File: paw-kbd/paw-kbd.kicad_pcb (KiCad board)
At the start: 2 copper layers, 130.8 x 88.1 mm, 55 parts, among them J1 OLED, J2 TRRS, J3 TRACKBALL, SW1 SW_PUSH, SW10 SW_PUSH, SW11 SW_PUSH, SW12 SW_PUSH, SW13 SW_PUSH, SW14 SW_PUSH, SW15 SW_PUSH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

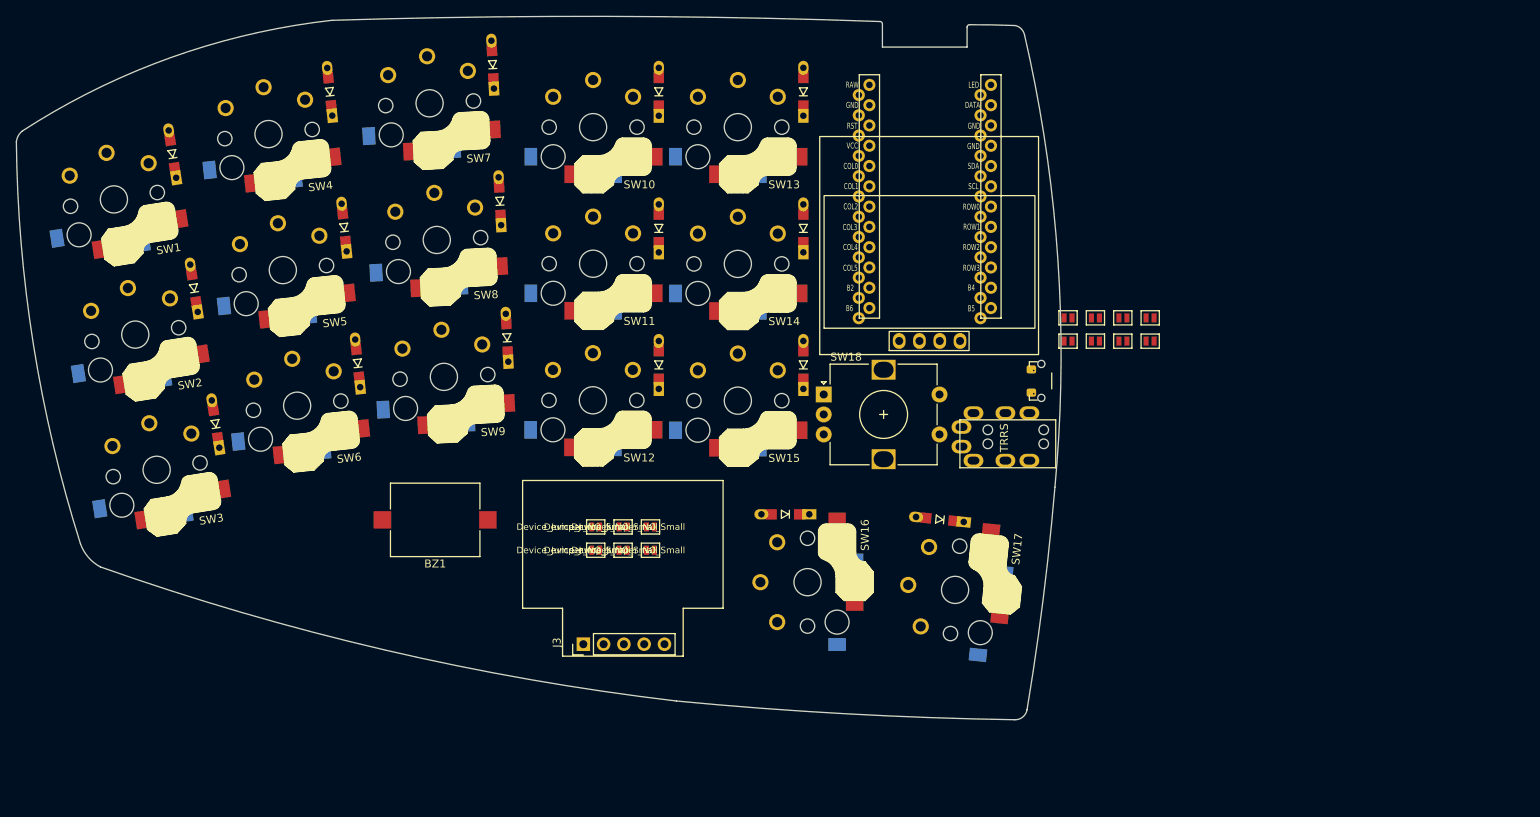
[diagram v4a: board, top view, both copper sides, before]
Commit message: big oled
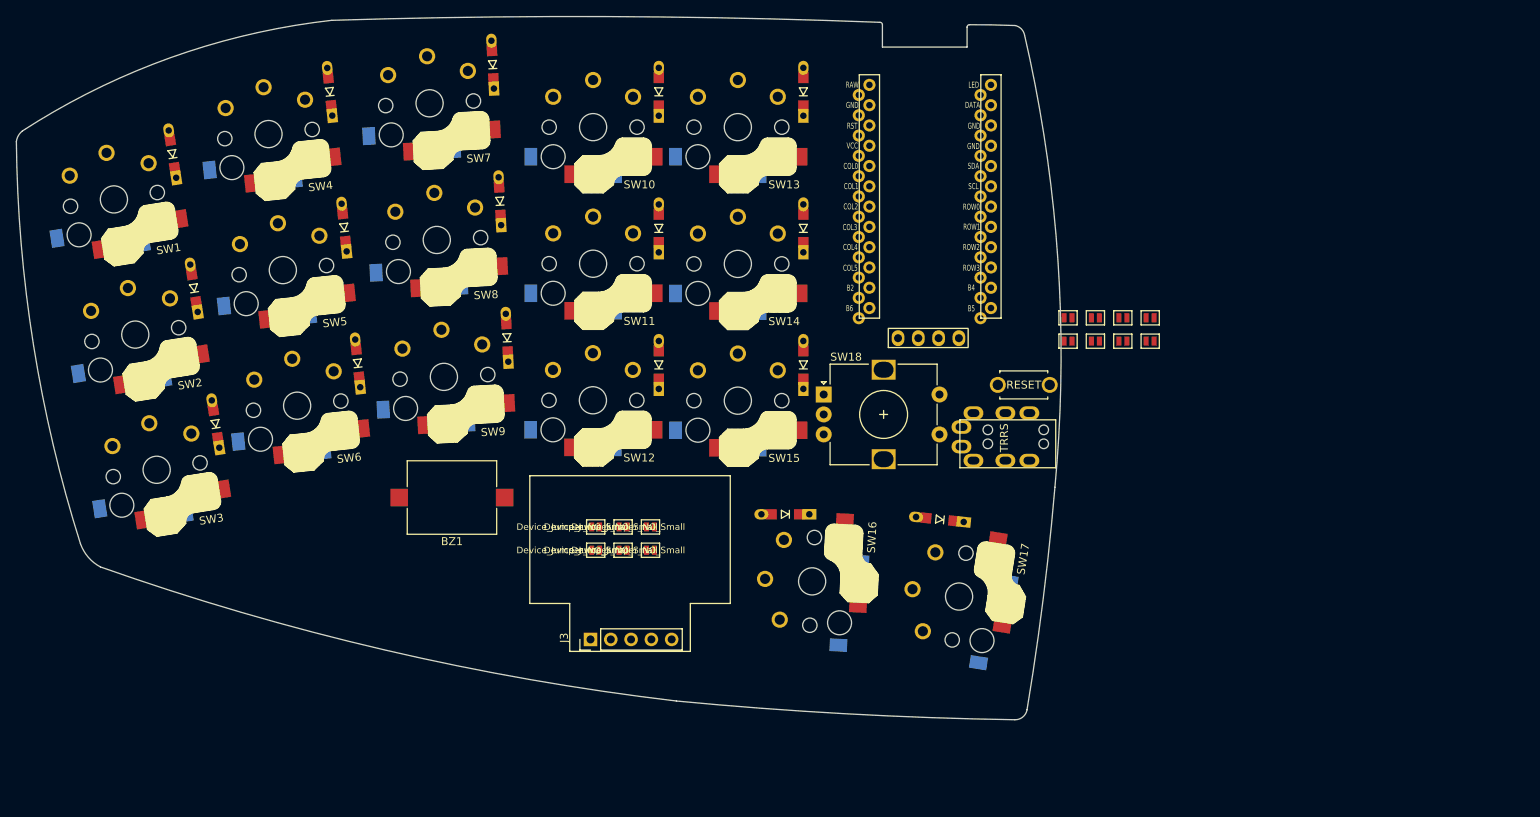
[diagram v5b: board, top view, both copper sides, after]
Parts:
- RSW1: footprint keeb-footprints:SW_Push_1P1T-MP_NO_Horizontal_both_sides -> kbd:ResetSW
- moved BZ1 3.50 mm to (139.5, 110.4)
- moved RSW1 2.26 mm to (211.1, 96.3), turned to 0 degrees
- moved J3 1.08 mm to (156.8, 128.2)
- moved SW17 0.97 mm to (203.0, 122.8), turned to 81 degrees
- moved SW16 0.58 mm to (184.6, 120.9), turned to 87 degrees
- moved J1 0.39 mm to (199.2, 80.4)
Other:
- board size 130.8 x 88.1 mm -> 130.8 x 88 mm

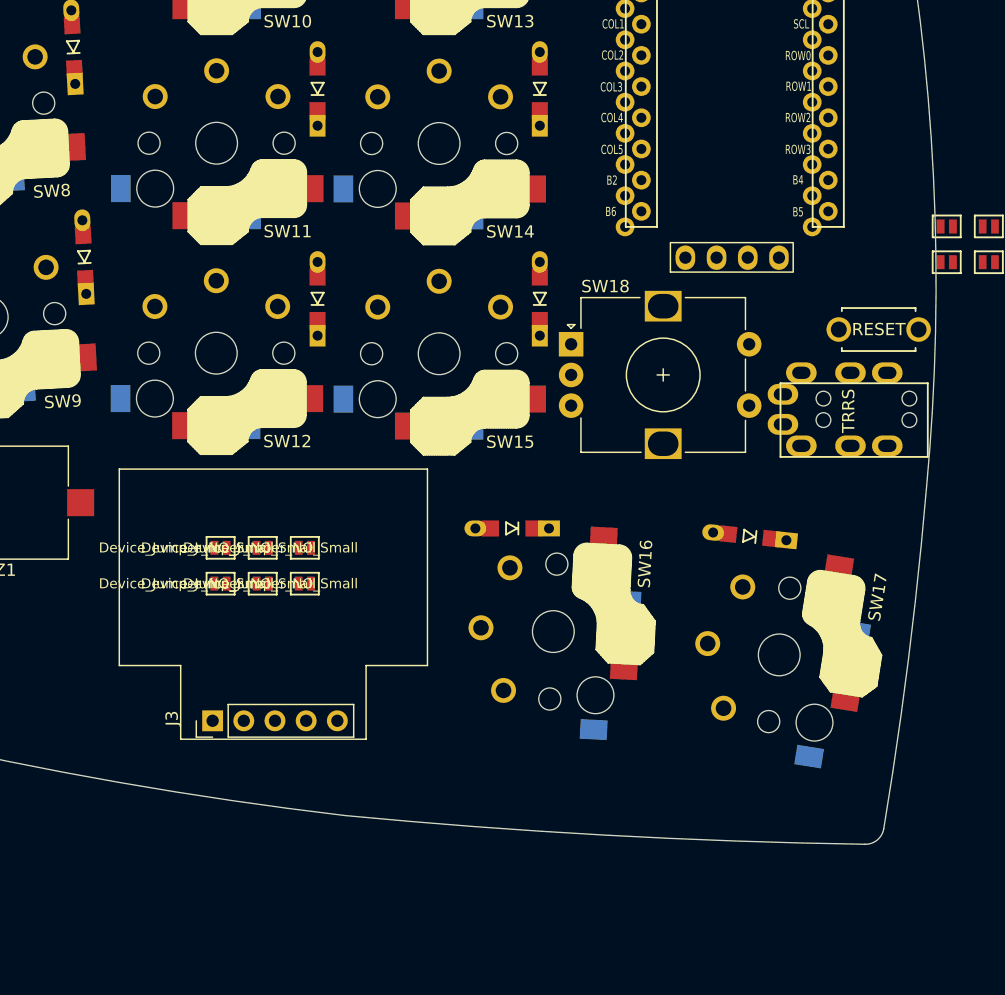
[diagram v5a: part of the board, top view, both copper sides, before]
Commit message: pimoroni trackball footprint
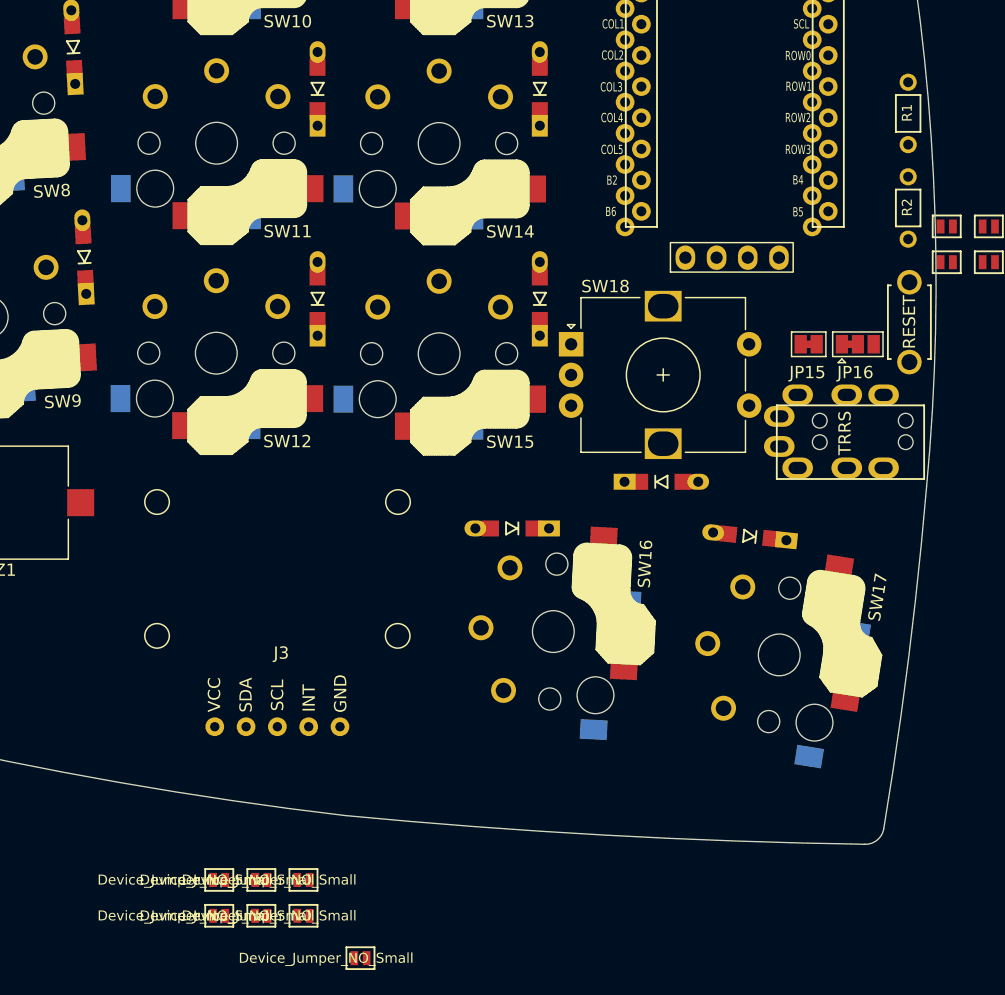
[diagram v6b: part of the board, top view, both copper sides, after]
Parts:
- added D18: DIODE, kbd:D3_TH_SMD_v2, F.Cu at (193.4, 108.7)
- added JP15: Jumper_2_Bridged, Jumper:SolderJumper-2_P1.3mm_Bridged_Pad1.0x1.5mm, F.Cu at (205.4, 97.5)
- added JP16: Jumper_3_Bridged12, Jumper:SolderJumper-3_P1.3mm_Bridged12_Pad1.0x1.5mm, F.Cu at (209.4, 97.5)
- added JP17: Device_Jumper_NO_Small, kbd:Jumper, F.Cu at (168.9, 147.5)
- added R1: R, kbd:R, F.Cu at (213.5, 78.7)
- added R2: R, kbd:R, F.Cu at (213.5, 86.4)
- J3: footprint keeb-footprints:pimoroni -> keeb-footprints:pimoroni_trackball
- moved JP11 27.1 mm to (160.8, 144.1)
- moved JP13 27.1 mm to (164.2, 144.1)
- moved JP9 27.1 mm to (157.4, 144.1)
- moved JP10 27.1 mm to (157.4, 141.1)
- moved JP12 27.1 mm to (164.2, 141.1)
- moved JP14 27.1 mm to (160.8, 141.1)
- moved J3 13.5 mm to (162.1, 115.8), turned to 0 degrees
- moved RSW1 2.57 mm to (213.6, 95.7), turned to 90 degrees
- moved J2 1.82 mm to (214.8, 105.5)
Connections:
- D1 pad 2: Net-(D1-Pad2) -> top
- D10 pad 2: Net-(D1-Pad2) -> top
- D11 pad 2: Net-(D11-Pad2) -> home
- D12 pad 2: Net-(D12-Pad2) -> bottom
- D14 pad 2: Net-(D1-Pad2) -> top
- D15 pad 2: Net-(D11-Pad2) -> home
- D16 pad 2: Net-(D12-Pad2) -> bottom
- D2 pad 2: Net-(D11-Pad2) -> home
- D3 pad 2: Net-(D12-Pad2) -> bottom
- D4 pad 2: Net-(D1-Pad2) -> top
- D5 pad 2: Net-(D11-Pad2) -> home
- D6 pad 2: Net-(D12-Pad2) -> bottom
- D7 pad 2: Net-(D1-Pad2) -> top
- D8 pad 2: Net-(D11-Pad2) -> home
- D9 pad 2: Net-(D12-Pad2) -> bottom
- J3 pad 1: Net-(J3-Pad1) -> Net-(JP11-Pad1)
- J3 pad 3: VCC -> Net-(J3-Pad3)
- J3 pad 4: Net-(J3-Pad4) -> Net-(JP14-Pad1)
- JP10 pad 1: Net-(J3-Pad2) -> Net-(J3-Pad3)
- JP11 pad 1: Net-(J3-Pad4) -> Net-(JP11-Pad1)
- JP11 pad 2: GND -> VCC
- JP12 pad 1: Net-(J3-Pad2) -> Net-(JP11-Pad1)
- JP13 pad 1: Net-(J3-Pad4) -> Net-(J3-Pad5)
- JP13 pad 2: SCL -> GND
- JP14 pad 1: Net-(J3-Pad5) -> Net-(JP14-Pad1)
- JP9 pad 1: Net-(J3-Pad1) -> Net-(J3-Pad2)
- SW1 pad 1: col1 -> pinky
- SW10 pad 1: col4 -> index
- SW11 pad 1: col4 -> index
- SW12 pad 1: col4 -> index
- SW13 pad 1: col5 -> far
- SW14 pad 1: col5 -> far
- SW15 pad 1: col5 -> far
- SW16 pad 1: col4 -> index
- SW17 pad 1: col5 -> far
- SW2 pad 1: col1 -> pinky
- SW3 pad 1: col1 -> pinky
- SW4 pad 1: col2 -> ring
- SW5 pad 1: col2 -> ring
- SW6 pad 1: col2 -> ring
- SW7 pad 1: col3 -> SW18A
- SW8 pad 1: col3 -> SW18A
- SW9 pad 1: col3 -> SW18A
- U1 pad 1: col5 -> AUDIO
- U1 pad 10: col1 -> ring
- U1 pad 11: col0 -> pinky
- U1 pad 12: thumb -> unconnected-(U1-Pad12)
- U1 pad 13: unconnected-(U1-Pad13) -> ENCA
- U1 pad 14: unconnected-(U1-Pad14) -> ENCB
- U1 pad 17: unconnected-(U1-Pad17) -> thumb
- U1 pad 7: col4 -> far
- U1 pad 8: col3 -> index
- U1 pad 9: col2 -> SW18A

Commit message: 2023-07-29 15:25:01
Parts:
- added D18: type="D" model="DIODE" lib="", kbd:D3_TH_SMD_v2, F.Cu at (244.2, 90.2)
- added SW18: SW_PUSH, keeb-footprints:ChocV1_V2_Hotswap_optional_reversed_choc_spacing, F.Cu at (204.9, 120.0)
- D1, D10, D11, D12, D13, D14, D15, D16, D17, D2, D3, D4, D5, D6, D7, D8, D9: value DIODE -> type="D" model="DIODE" lib=""
- SW16, SW17: footprint keeb-footprints:ChocV1_V2_Hotswap_optional_reversed_15u_choc_spacing -> keeb-footprints:ChocV1_V2_Hotswap_optional_reversed_choc_spacing
- moved BZ1 122.3 mm to (256.6, 75.0)
- moved JP17 99.1 mm to (267.5, 137.8)
- moved JP10 99.1 mm to (256.0, 131.4)
- moved JP9 99.1 mm to (256.0, 134.3)
- moved JP11 99.1 mm to (259.4, 134.3)
- moved JP12 99.1 mm to (262.8, 131.4)
- moved JP13 99.1 mm to (262.8, 134.3)
- moved JP14 99.1 mm to (259.4, 131.4)
- moved J3 87.1 mm to (248.9, 109.2)
- moved D16 78.1 mm to (256.8, 93.0)
- moved D18 31.3 mm to (223.5, 100.0)
- moved D17 26.2 mm to (226.5, 109.5)
- moved SW17 16.6 mm to (187.3, 117.4), turned to 84 degrees
- moved SW16 15.9 mm to (169.3, 116.5), turned to 90 degrees
- renumbered SW18 to SW19
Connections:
- SW16 pad 1: index -> middle
- SW17 pad 1: far -> index
- SW19 pad S1: SW18A -> SW19A
- SW19 pad S2: SW18B -> SW19B
- SW7 pad 1: SW18A -> middle
- SW8 pad 1: SW18A -> middle
- SW9 pad 1: SW18A -> middle
- U1 pad 9: SW18A -> middle

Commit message: 2023-07-29 21:57:05
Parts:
- moved SW16 3.50 mm to (166.0, 115.3), turned to 0 degrees
- moved SW17 2.56 mm to (185.0, 116.3), turned to -6 degrees
- moved SW18 1.14 mm to (203.9, 119.4), turned to -13 degrees
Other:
- board size 130.8 x 88 mm -> 131 x 80.7 mm
